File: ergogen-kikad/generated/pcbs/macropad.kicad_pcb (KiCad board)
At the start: 2 copper layers, 114.2 x 55 mm, 22 parts, among them J1 JST-PH S2B-PH-K-S

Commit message: Move outer M2 mounts between fifth keys and controls
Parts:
- moved H5 28.5 mm to (256.4, 129.8)
- moved H6 28.5 mm to (256.4, 167.2)

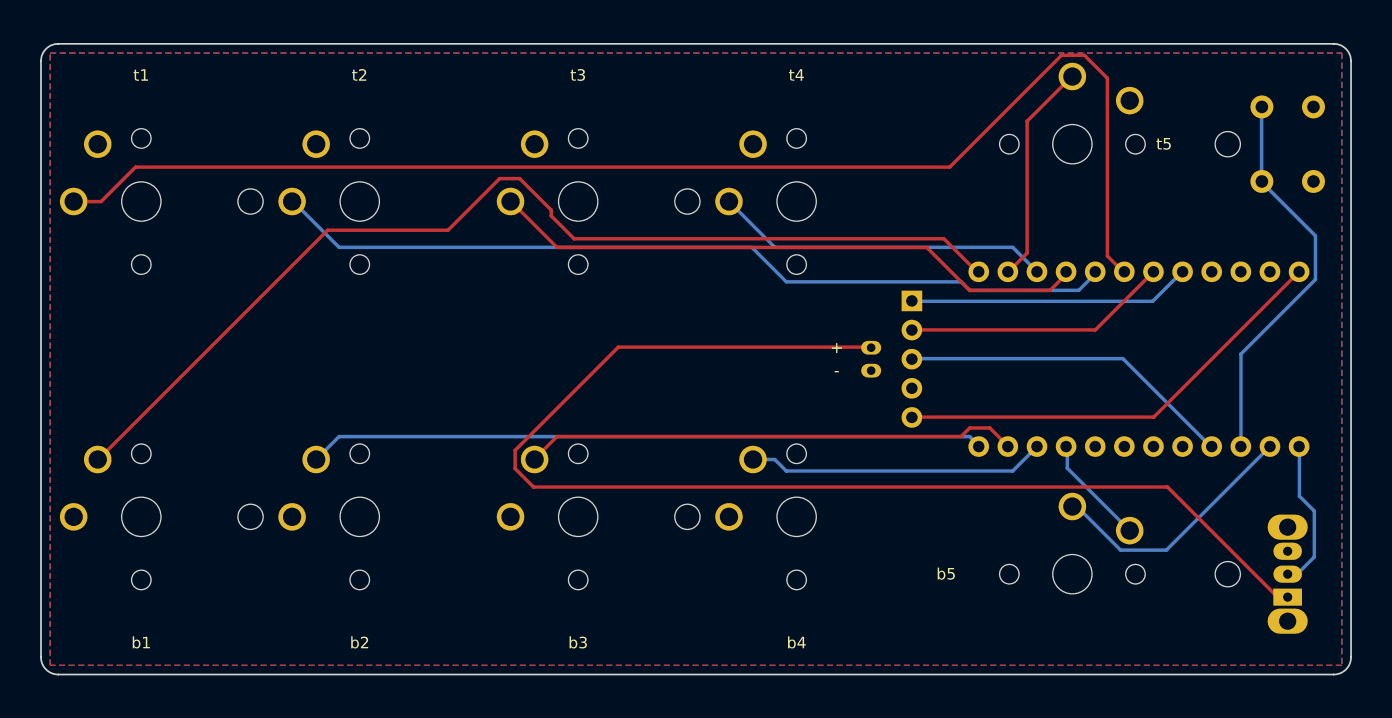
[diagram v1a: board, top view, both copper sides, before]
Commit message: Recess original battery through main PCB onto intact baseplate
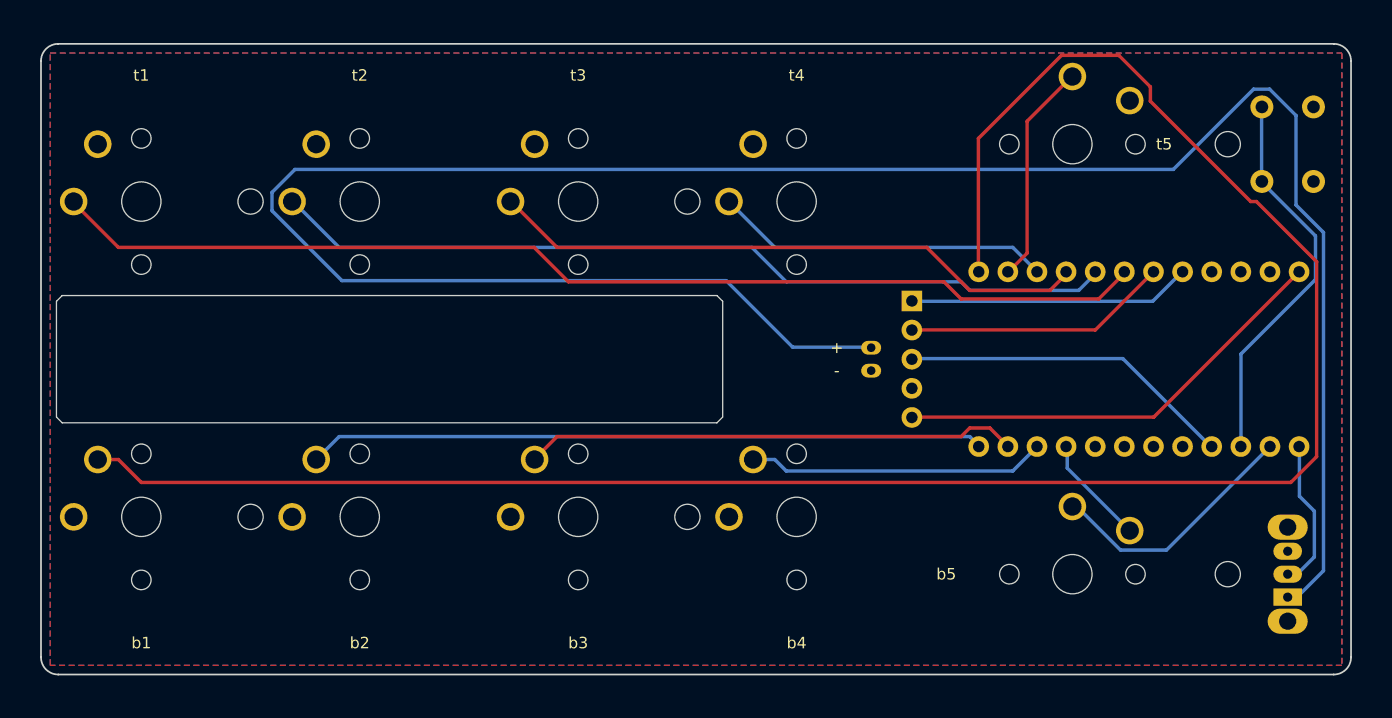
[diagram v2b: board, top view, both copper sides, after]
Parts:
- added WELL1: Battery well 58.1x11.1, Battery_Well, F.Cu at (183.3, 148.5)
- BAT1: value 301055 220mAh max 57.5x10.5x3.5 -> 301055 220mAh max 57.5x10.5x3.5 z=-1.4
- moved BAT1 0.75 mm to (183.3, 148.5)
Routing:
- net BAT_POS: track 108.5 -> 197.6 mm
- net P9: track 90.8 -> 177.6 mm
- net P4: track 114.2 -> 96.4 mm

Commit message: Shift outer screws left to clear control housings
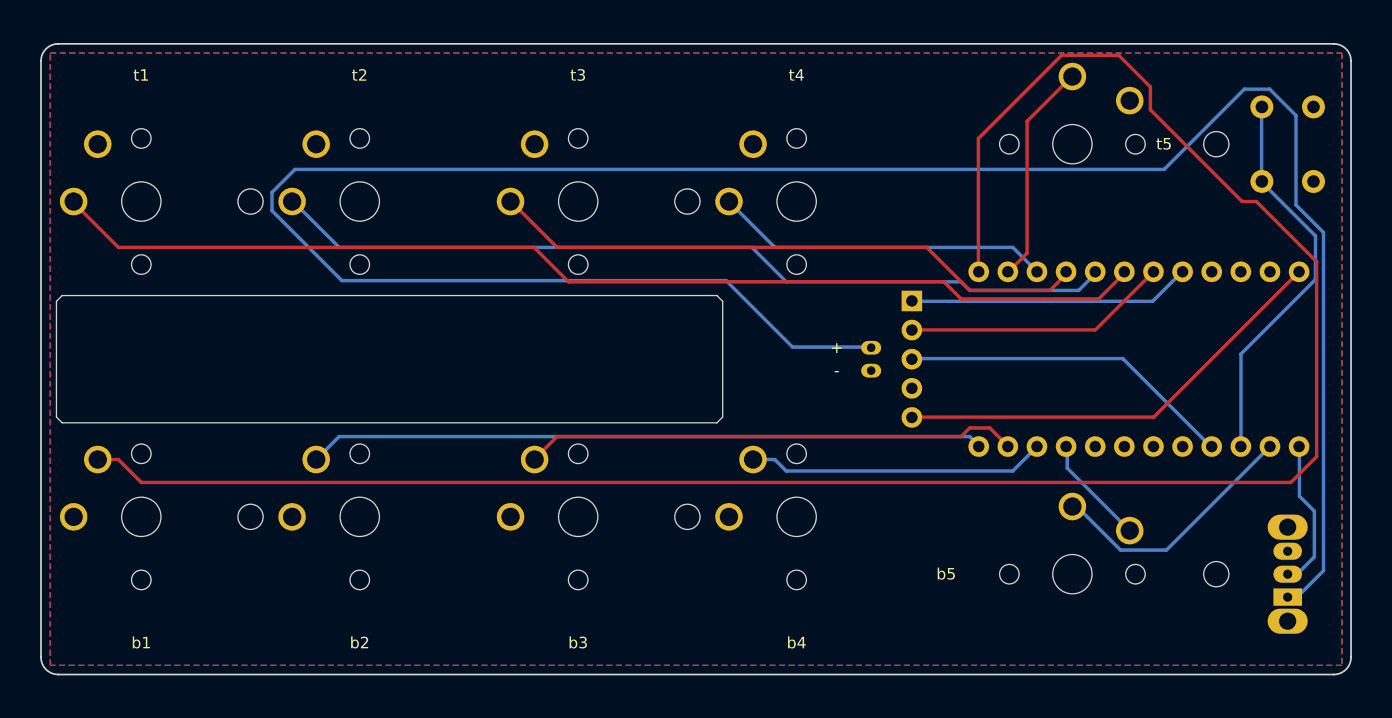
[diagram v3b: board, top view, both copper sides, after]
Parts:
- moved H5 1.00 mm to (255.4, 129.8)
- moved H6 1.00 mm to (255.4, 167.2)

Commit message: Add PCB border for top-mounted case and move outer screws inward
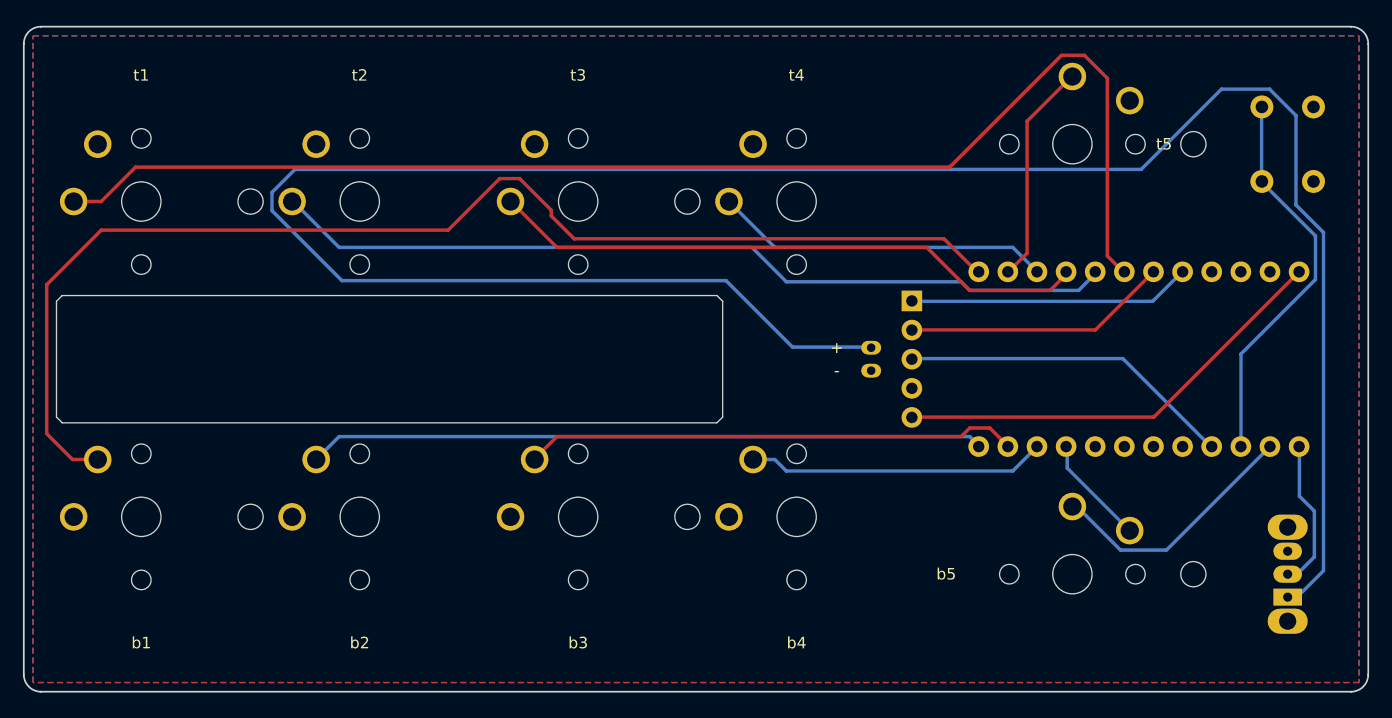
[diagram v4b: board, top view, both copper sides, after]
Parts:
- moved H5 2.00 mm to (253.4, 129.8)
- moved H6 2.00 mm to (253.4, 167.2)
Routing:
- net P9: track 178.1 -> 107.4 mm
- net P4: track 96.4 -> 114.2 mm
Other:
- board size 114.2 x 55 mm -> 117.2 x 58 mm

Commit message: Route XIAO Plus board with recessed mounting and RF clearance
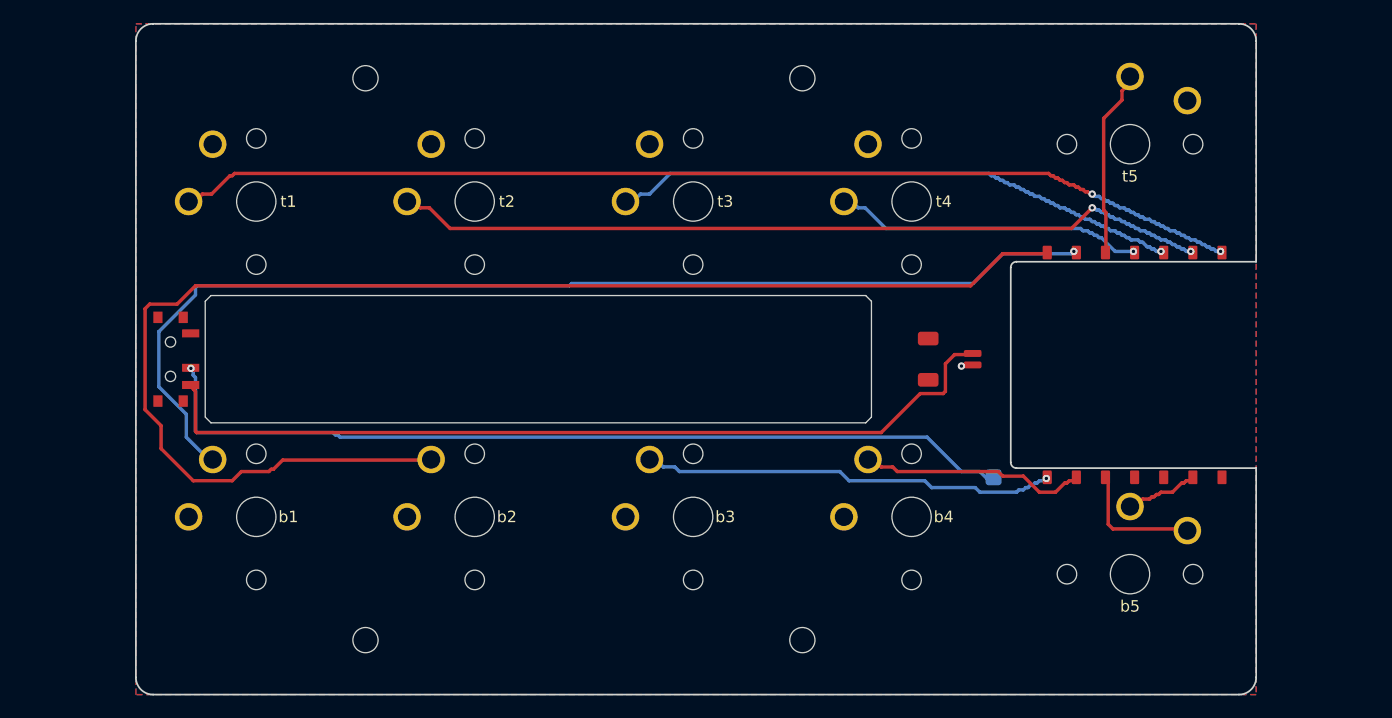
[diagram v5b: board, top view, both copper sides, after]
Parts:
- removed H5, H6: M2 mount, M2_Mount
- removed LCD1: nice!view, Nice_View_Socketed_Module
- removed RST1: 6mm top-actuated tactile, SW_PUSH_6mm_H4_3mm
- added BW1: Insulated lead to XIAO BAT+ underside, XIAO_Underside_BAT_Wire_Landing, B.Cu at (235.9, 158.8)
- J1: value JST-PH S2B-PH-K-S -> JST-SH 2-pin horizontal; footprint JST_PH_S2B_PH_K_Horizontal -> JST_SH_SM02B_SRSS_TB_Horizontal
- MCU1: value nice!nano v2 -> XIAO nRF52840 Plus edge-soldered; footprint Nice_Nano_V2 -> XIAO_nRF52840_Plus_Coplanar_Edge_Solder
- PWR1: value OS102011MS2QN1 -> PCM12SMTR side power; footprint CK_OS102011MS2QN1 -> CK_PCM12SMTR
- S10, S9: value Choc v1 1.5U -> Choc v1 1U; footprint PG1350_1_5U -> PG1350_1U
- moved PWR1 98.9 mm to (164.5, 148.5), turned to -90 degrees
- moved H1 14.7 mm to (181.2, 124.0)
- moved H2 14.7 mm to (219.3, 124.0)
- moved H3 14.7 mm to (181.2, 173.0)
- moved H4 14.7 mm to (219.3, 173.0)
- moved BAT1 13.0 mm to (196.2, 148.5)
- moved WELL1 13.0 mm to (196.2, 148.5)
- moved S1 10.0 mm to (171.7, 134.8)
- moved S3 10.0 mm to (209.8, 134.8)
- moved S4 10.0 mm to (228.8, 134.8)
- moved S5 10.0 mm to (171.7, 162.2)
- moved S7 10.0 mm to (209.8, 162.2)
- moved S8 10.0 mm to (228.8, 162.2)
- moved S2 10.0 mm to (190.7, 134.8)
- moved S6 10.0 mm to (190.7, 162.2)
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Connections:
- MCU1 pad 1: LCD_CS -> D0
- MCU1 pad 10: P7 -> D9
- MCU1 pad 11: P8 -> D10
- MCU1 pad 12: P9 -> 3V3
- MCU1 pad 13: P10 -> GND
- MCU1 pad 14: P16 -> VBUS
- MCU1 pad 2: (no net) -> D1
- MCU1 pad 3: GND -> D2
- MCU1 pad 4: GND -> D3
- MCU1 pad 5: LCD_SI -> D4
- MCU1 pad 6: LCD_CLK -> D5
- MCU1 pad 7: P4 -> D6
- MCU1 pad 8: P5 -> D7
- MCU1 pad 9: P6 -> D8
- PWR1 pad 1: BAT_POS -> (no net)
- PWR1 pad 3: (no net) -> BAT_POS
- S1 pad 2: P4 -> D0
- S10 pad 1: P15 -> D9
- S2 pad 2: P5 -> D1
- S3 pad 2: P6 -> D2
- S4 pad 2: P7 -> D3
- S5 pad 1: P9 -> D5
- S6 pad 1: P10 -> D6
- S7 pad 1: P16 -> D7
- S8 pad 1: P14 -> D8
- S9 pad 2: P8 -> D4
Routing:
- net BAT_POS: track 197.6 -> 76.5 mm
- net D6: track 0.00 -> 119.1 mm
- net P4: track 114.2 -> 0.00 mm
- net P9: track 107.4 -> 0.00 mm
- net D5: track 0.00 -> 96.8 mm, vias 0 -> 1
- net D0: track 0.00 -> 94.3 mm, vias 0 -> 2
- net P5: track 74.1 -> 0.00 mm
- net D1: track 0.00 -> 72.2 mm, vias 0 -> 2
- net VBAT: track 13.1 -> 77.1 mm, vias 0 -> 1
- net P10: track 59.0 -> 0.00 mm
- net P6: track 52.5 -> 0.00 mm
- net D2: track 0.00 -> 50.9 mm, vias 0 -> 1
- net P16: track 43.2 -> 0.00 mm
- net LCD_CS: track 39.1 -> 0.00 mm
- net D7: track 0.00 -> 36.4 mm, vias 0 -> 1
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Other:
- board size 117.2 x 58 mm -> 97.7 x 58.5 mm
